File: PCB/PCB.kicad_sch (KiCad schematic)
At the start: 20 parts, among them SW1 SW_Push, SW2 SW_Push, SW3 SW_Push, SW4 SW_Push, SW5 SW_Push, SW6 SW_Push, U1 NodeMCU_1.0_(ESP-12E)

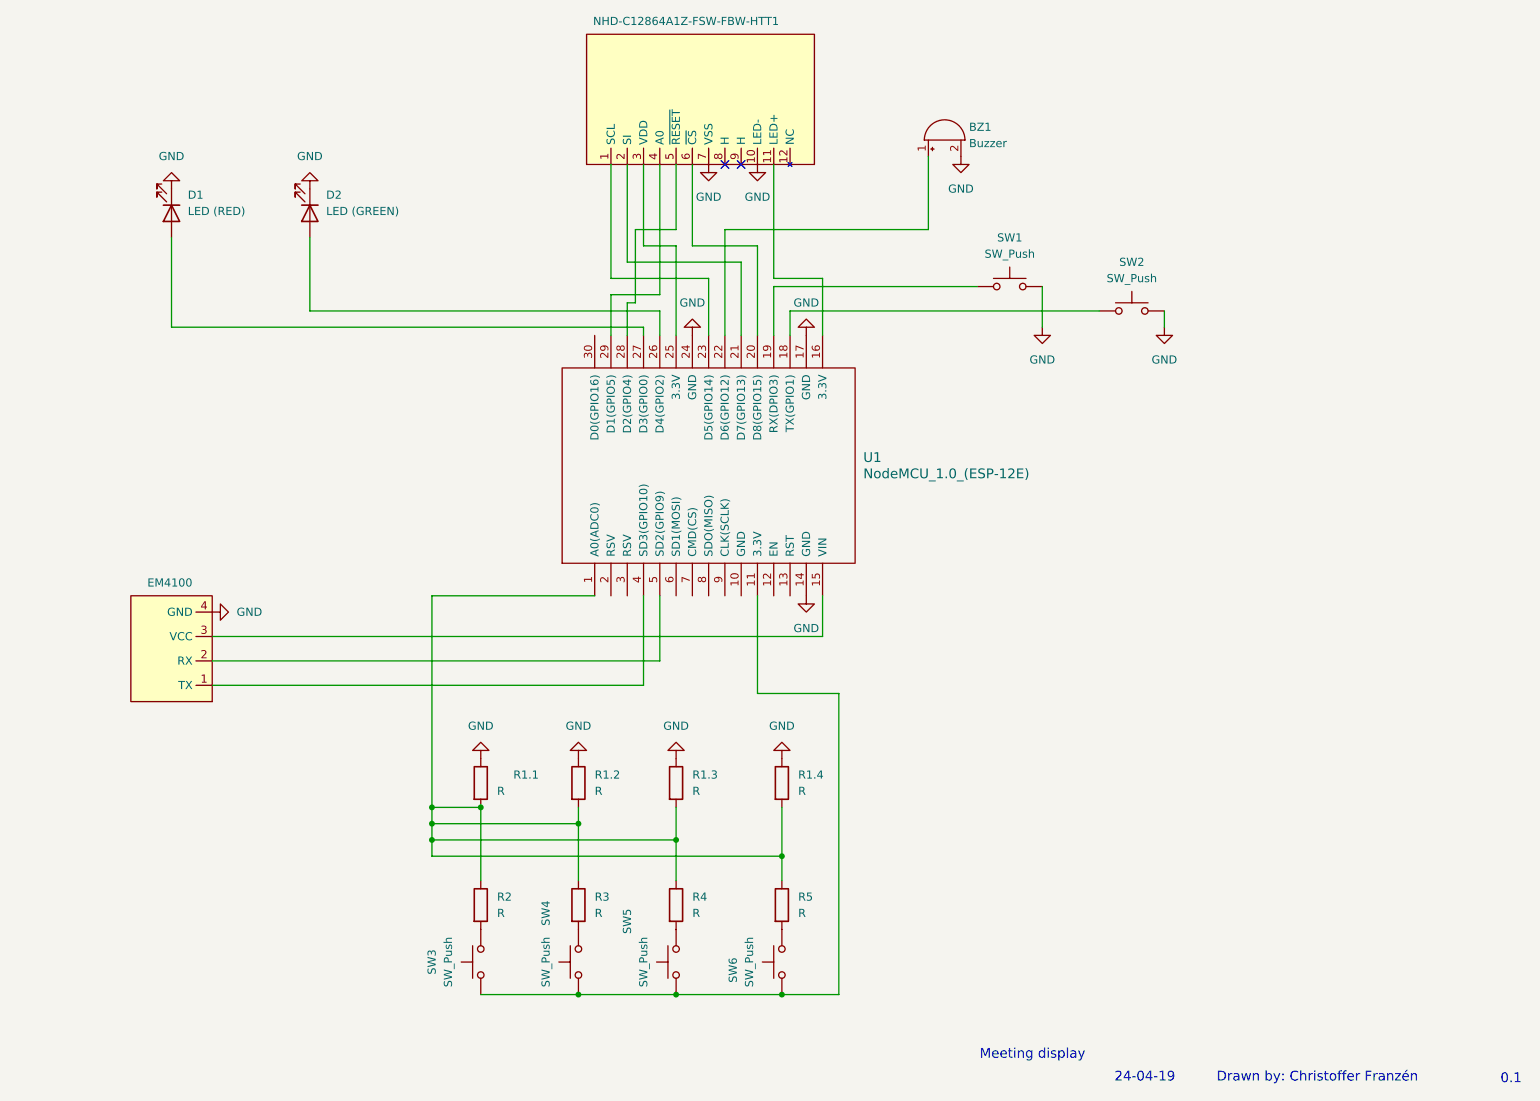
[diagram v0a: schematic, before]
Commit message: updated scematic and added footprints
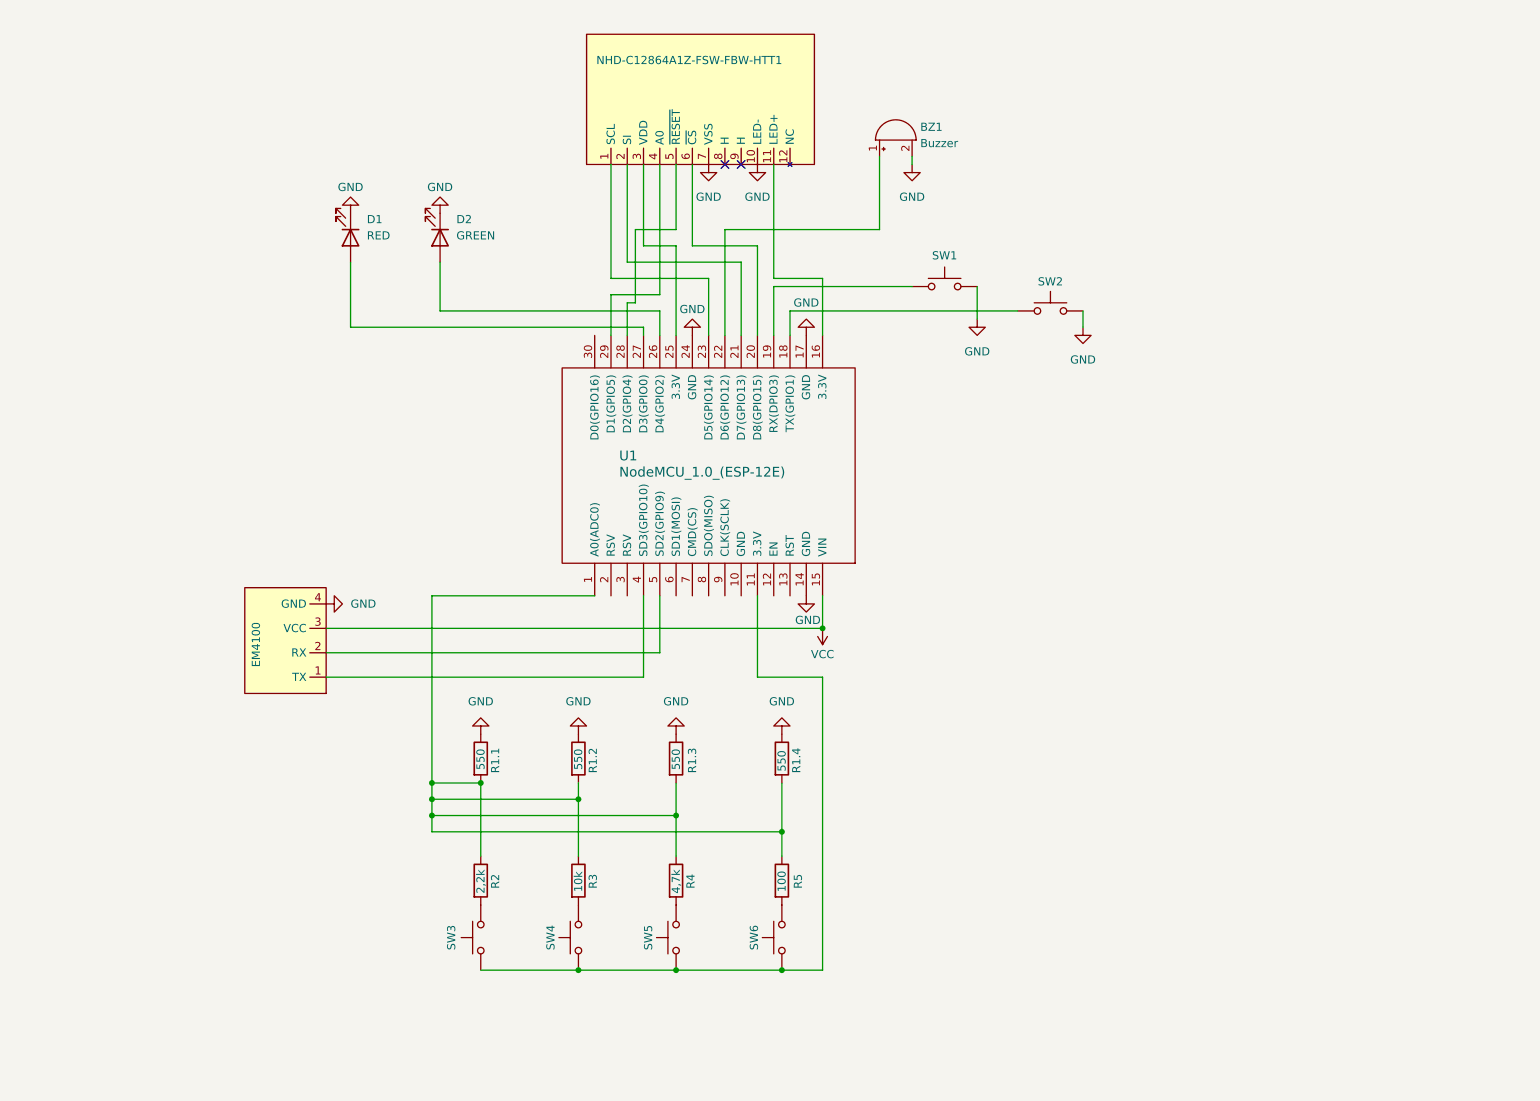
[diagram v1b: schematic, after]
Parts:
- BZ1: footprint (none) -> Buzzer_Beeper:Buzzer_12x9.5RM7.6
- D1: value LED (RED) -> RED; footprint (none) -> Diode_SMD:D_1206_3216Metric_Pad1.42x1.75mm_HandSolder
- D2: value LED (GREEN) -> GREEN; footprint (none) -> Diode_SMD:D_1206_3216Metric_Pad1.42x1.75mm_HandSolder
- EM4100: footprint (none) -> Connector:NS-Tech_Grove_1x04_P2mm_Vertical
- R1.1, R1.2, R1.3, R1.4: value R -> 550; footprint (none) -> Resistor_SMD:R_1206_3216Metric_Pad1.30x1.75mm_HandSolder
- R2: value R -> 2,2k; footprint (none) -> Resistor_SMD:R_1206_3216Metric_Pad1.30x1.75mm_HandSolder
- R3: value R -> 10k; footprint (none) -> Resistor_SMD:R_1206_3216Metric_Pad1.30x1.75mm_HandSolder
- R4: value R -> 4,7k; footprint (none) -> Resistor_SMD:R_1206_3216Metric_Pad1.30x1.75mm_HandSolder
- R5: value R -> 100; footprint (none) -> Resistor_SMD:R_1206_3216Metric_Pad1.30x1.75mm_HandSolder
- SW1, SW2, SW3, SW4, SW5, SW6: footprint (none) -> Button_Switch_SMD:SW_Push_SPST_NO_Alps_SKRK
- U1: footprint (none) -> 113990105:NodeMCU
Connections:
- net VCC: now reaches EM4100.3 (VCC), U1.15 (VIN)
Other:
- note removed: "0.1"
- note removed: "24-04-19"
- note removed: "Drawn by: Christoffer Franzén"
- note removed: "Meeting display"
- company: (none) -> KTH
- title: (none) -> Meeting display
- moved on the sheet: BZ1, D1, D2, EM4100, R1.1, R1.2, R1.3, R1.4, R2, R3, R4, R5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

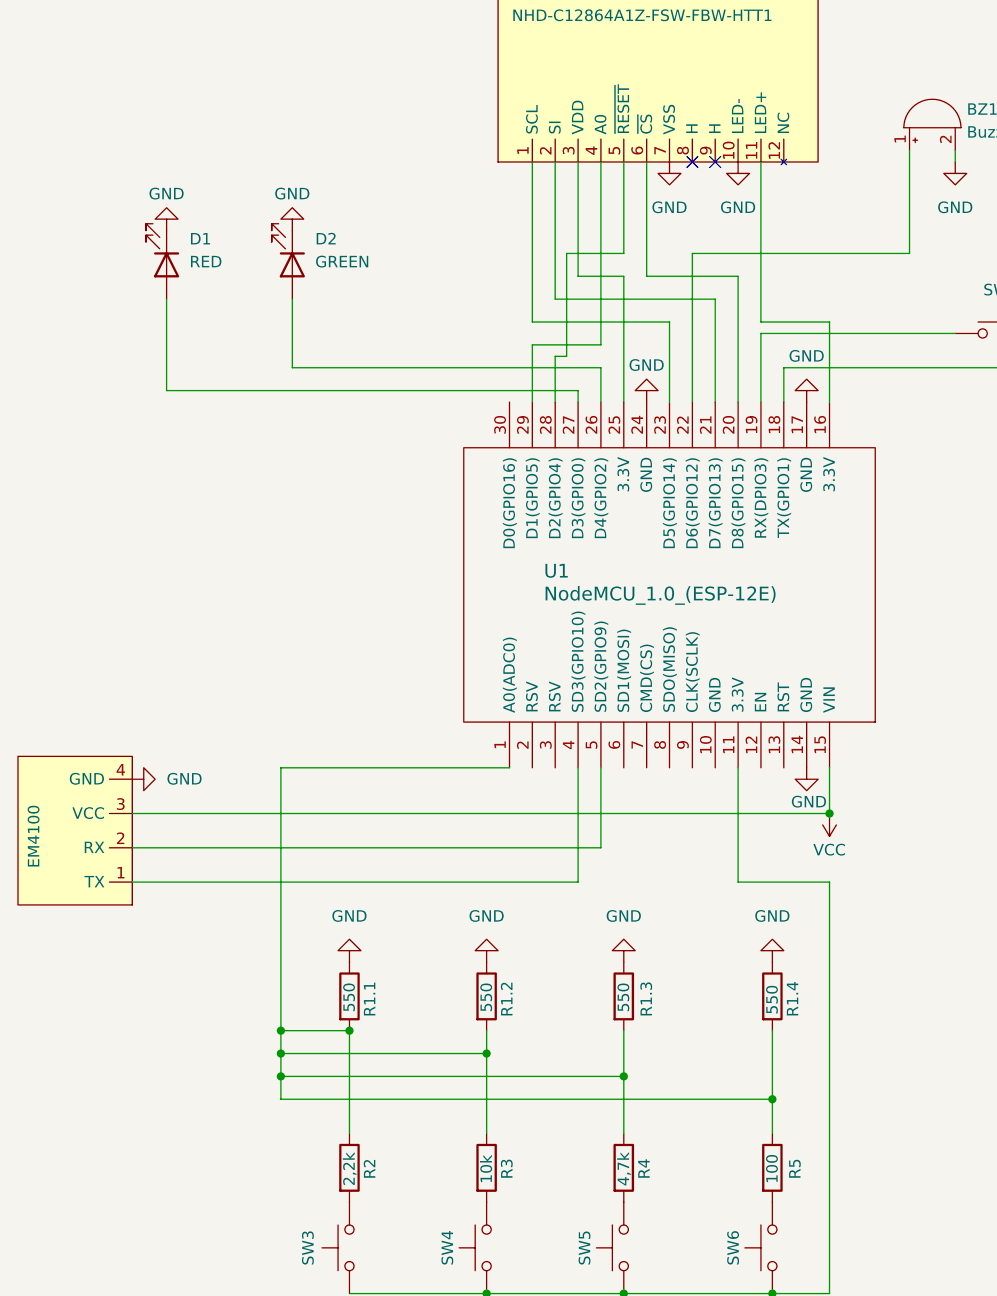
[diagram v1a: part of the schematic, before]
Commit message: version 0.2 removed resistor and 3v run
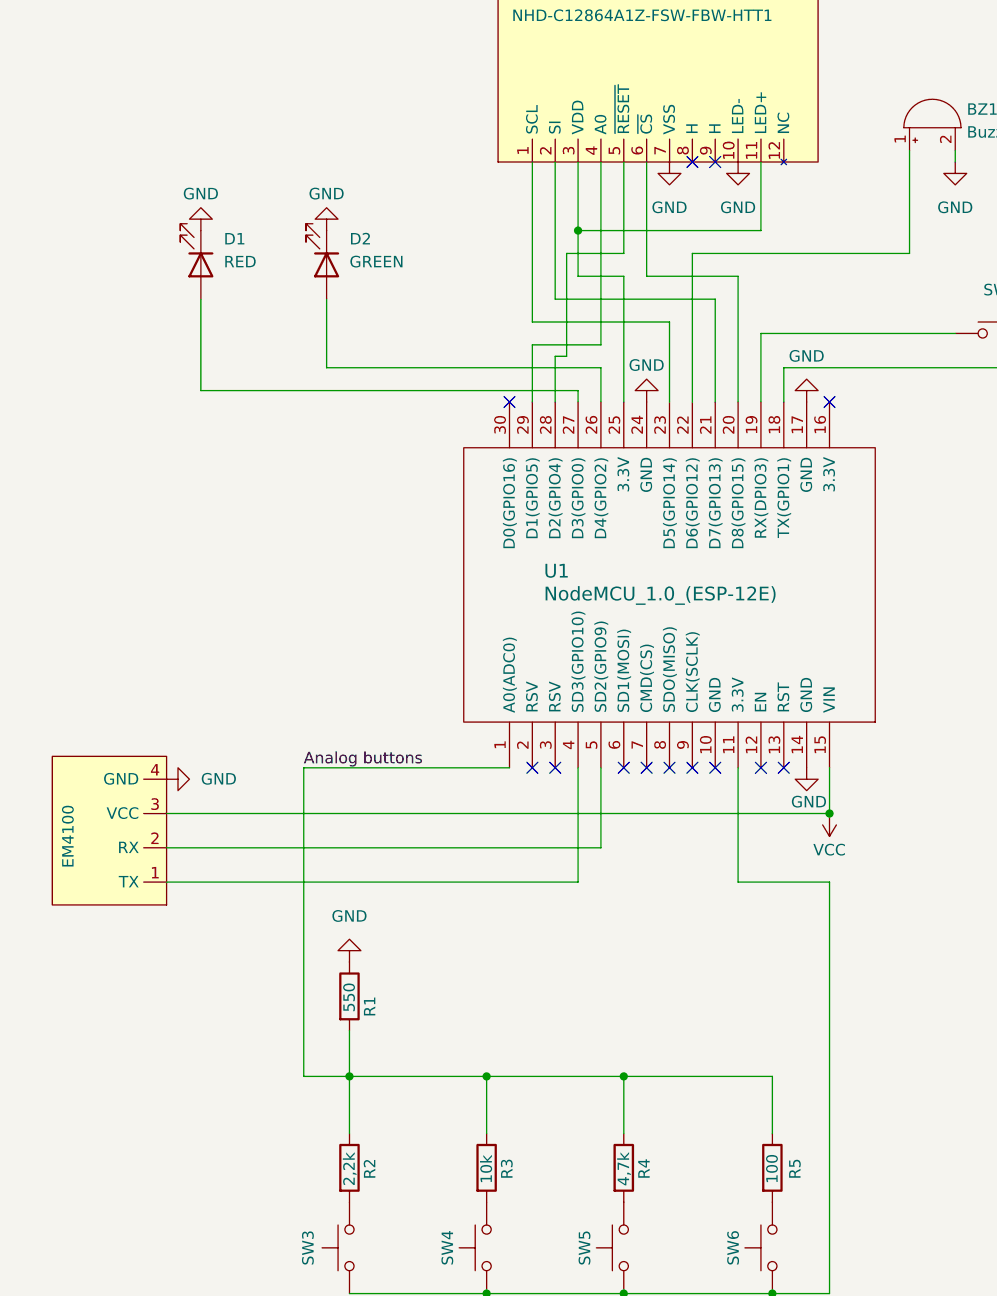
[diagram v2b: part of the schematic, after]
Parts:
- removed R1.2, R1.3, R1.4: 550, Resistor_SMD:R_1206_3216Metric_Pad1.30x1.75mm_HandSolder, symbol Device:R
- NHD-C12864A1Z-FSW-FBW-HTT1: footprint (none) -> Connector_PinHeader_1.27mm:PinHeader_1x30_P1.27mm_Horizontal
- renumbered R1.1 to R1
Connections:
- net Analog buttons: now reaches R1.2, R2.1, R3.1, R4.1, R5.1, U1.1 (A0(ADC0))
- net at NHD-C12864A1Z-FSW-FBW-HTT1.11 (LED+): now also NHD-C12864A1Z-FSW-FBW-HTT1.3 (VDD), U1.25 (3.3V); no longer U1.16 (3.3V)
- no-connect marks 2 -> 13
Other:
- moved on the sheet: D1, D2, EM4100

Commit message: added screen and button footprints
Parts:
- D1, D2: footprint Diode_SMD:D_1206_3216Metric_Pad1.42x1.75mm_HandSolder -> LED_THT:LED_D5.0mm
- NHD-C12864A1Z-FSW-FBW-HTT1: footprint Connector_PinHeader_1.27mm:PinHeader_1x30_P1.27mm_Horizontal -> Custom:NHD
- SW1, SW2, SW3, SW4, SW5, SW6: footprint Button_Switch_SMD:SW_Push_SPST_NO_Alps_SKRK -> Custom:SW_BUTT-2
- U1: footprint 113990105:NodeMCU -> Custom:NodeMCU
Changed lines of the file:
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@@
 			)
 		)
-		(property "Footprint" "Diode_SMD:D_1206_3216Metric_Pad1.42x1.75mm_HandSolder"
+		(property "Footprint" "LED_THT:LED_D5.0mm"
 			(at 92.71 62.23 0)
 			(effects
@@
 			)
 		)
-		(property "Footprint" "Button_Switch_SMD:SW_Push_SPST_NO_Alps_SKRK"
+		(property "Footprint" "Custom:SW_BUTT-2"
 			(at 181.61 64.77 0)
 			(effects
@@
 			)
 		)
-		(property "Footprint" "Connector_PinHeader_1.27mm:PinHeader_1x30_P1.27mm_Horizontal"
+		(property "Footprint" "Custom:NHD"
 			(at 128.778 14.986 0)
 			(effects
@@
 			)
 		)
-		(property "Footprint" "Button_Switch_SMD:SW_Push_SPST_NO_Alps_SKRK"
+		(property "Footprint" "Custom:SW_BUTT-2"
 			(at 151.13 171.45 0)
 			(effects
@@
 			)
 		)
-		(property "Footprint" "Button_Switch_SMD:SW_Push_SPST_NO_Alps_SKRK"
+		(property "Footprint" "Custom:SW_BUTT-2"
 			(at 198.12 68.58 0)
 			(effects
@@
 			)
 		)
-		(property "Footprint" "Button_Switch_SMD:SW_Push_SPST_NO_Alps_SKRK"
+		(property "Footprint" "Custom:SW_BUTT-2"
 			(at 134.62 171.45 0)
 			(effects
@@
 			)
 		)
-		(property "Footprint" "Button_Switch_SMD:SW_Push_SPST_NO_Alps_SKRK"
+		(property "Footprint" "Custom:SW_BUTT-2"
 			(at 119.38 171.45 0)
 			(effects
@@
 			)
 		)
-		(property "Footprint" "Button_Switch_SMD:SW_Push_SPST_NO_Alps_SKRK"
+		(property "Footprint" "Custom:SW_BUTT-2"
 			(at 104.14 171.45 0)
 			(effects
@@
 			)
 		)
-		(property "Footprint" "113990105:NodeMCU"
+		(property "Footprint" "Custom:NodeMCU"
 			(at 166.37 113.03 0)
 			(effects
@@
 			)
 		)
-		(property "Footprint" "Diode_SMD:D_1206_3216Metric_Pad1.42x1.75mm_HandSolder"
+		(property "Footprint" "LED_THT:LED_D5.0mm"
 			(at 106.68 62.23 0)
 			(effects

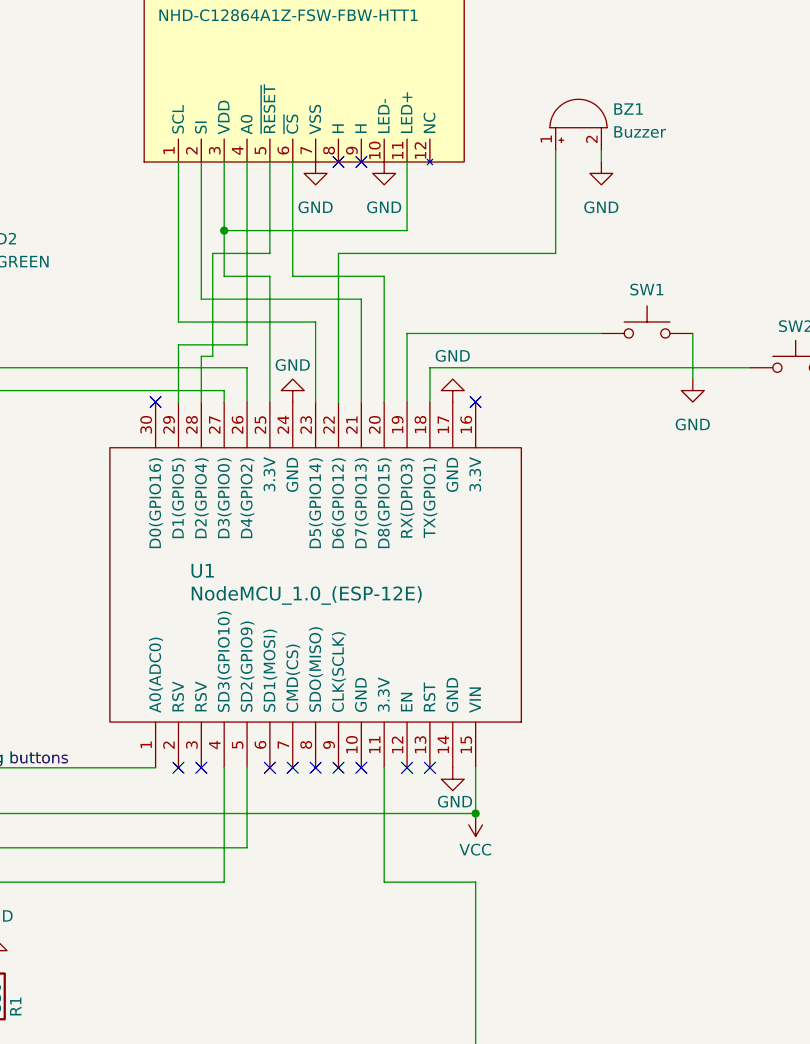
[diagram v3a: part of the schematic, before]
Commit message: done pcb drawing
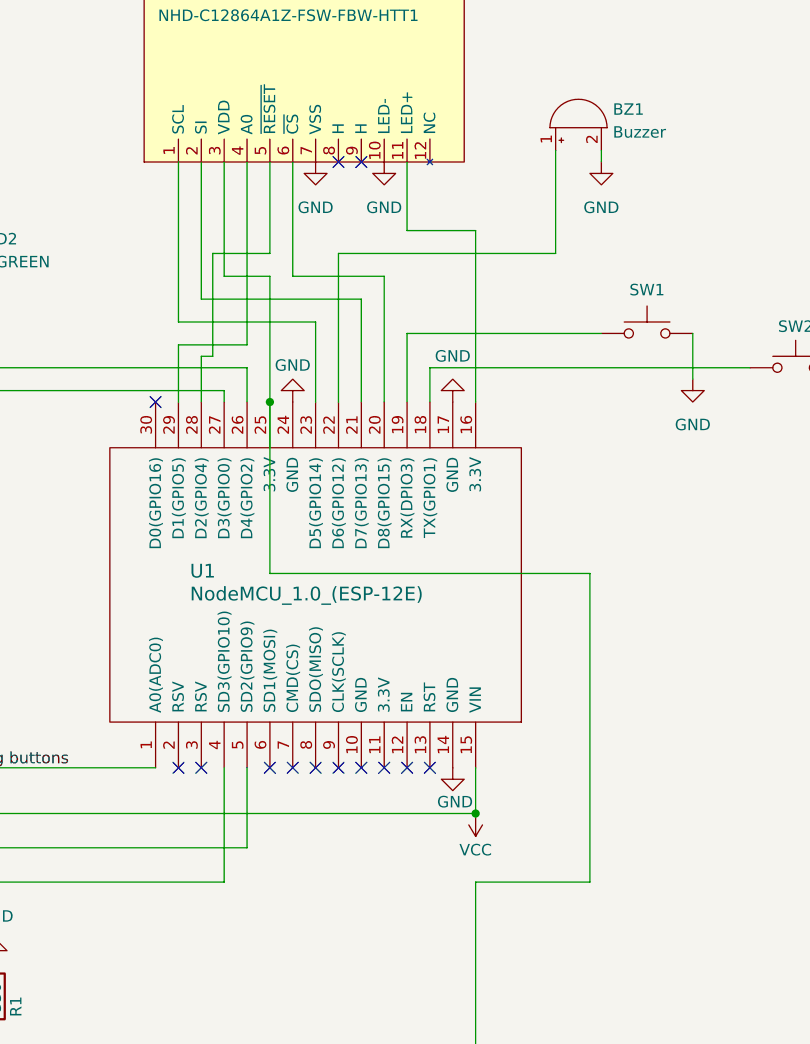
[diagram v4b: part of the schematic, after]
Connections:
- net at NHD-C12864A1Z-FSW-FBW-HTT1.3 (VDD), U1.25 (3.3V): now also SW3.1, SW4.1, SW5.1, SW6.1; no longer NHD-C12864A1Z-FSW-FBW-HTT1.11 (LED+)
- net at U1.16 (3.3V): now also NHD-C12864A1Z-FSW-FBW-HTT1.11 (LED+)
- now unconnected: U1.11 (3.3V)
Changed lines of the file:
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@@
-	)
-	(junction
-		(at 134.62 58.42)
-		(diameter 0)
-		(color 0 0 0 0)
 	)
 	(junction
@@
 	)
 	(junction
+		(at 139.7 77.47)
+		(diameter 0)
+		(color 0 0 0 0)
+	)
+	(junction
 		(at 109.22 152.4)
 		(diameter 0)
@@
 	)
 	(no_connect
+		(at 152.4 118.11)
+	)
+	(no_connect
 		(at 147.32 118.11)
 	)
@@
 	)
 	(no_connect
-		(at 162.56 77.47)
-	)
-	(no_connect
 		(at 149.86 50.8)
 	)
@@
 	(wire
 		(pts
+			(xy 162.56 58.42) (xy 154.94 58.42)
+		)
+		(stroke
+			(width 0)
+			(type default)
+		)
+	)
+	(wire
+		(pts
 			(xy 106.68 73.66) (xy 137.16 73.66)
 		)
@@
 	(wire
 		(pts
+			(xy 162.56 77.47) (xy 162.56 58.42)
+		)
+		(stroke
+			(width 0)
+			(type default)
+		)
+	)
+	(wire
+		(pts
 			(xy 156.21 176.53) (xy 162.56 176.53)
 		)
@@
 	(wire
 		(pts
+			(xy 162.56 130.81) (xy 175.26 130.81)
+		)
+		(stroke
+			(width 0)
+			(type default)
+		)
+	)
+	(wire
+		(pts
 			(xy 134.62 76.2) (xy 92.71 76.2)
 		)
@@
 	(wire
 		(pts
-			(xy 162.56 130.81) (xy 152.4 130.81)
-		)
-		(stroke
-			(width 0)
-			(type default)
-		)
-	)
-	(wire
-		(pts
 			(xy 154.94 77.47) (xy 154.94 69.85)
 		)
@@
 	(wire
 		(pts
-			(xy 134.62 58.42) (xy 134.62 50.8)
+			(xy 134.62 50.8) (xy 134.62 63.5)
 		)
 		(stroke
@@
 	(wire
 		(pts
+			(xy 139.7 96.52) (xy 139.7 77.47)
+		)
+		(stroke
+			(width 0)
+			(type default)
+		)
+	)
+	(wire
+		(pts
 			(xy 129.54 68.58) (xy 144.78 68.58)
 		)
@@
 	(wire
 		(pts
+			(xy 175.26 96.52) (xy 139.7 96.52)
+		)
+		(stroke
+			(width 0)
+			(type default)
+		)
+	)
+	(wire
+		(pts
 			(xy 134.62 77.47) (xy 134.62 76.2)
 		)
@@
 	(wire
 		(pts
-			(xy 134.62 63.5) (xy 134.62 58.42)
-		)
-		(stroke
-			(width 0)
-			(type default)
-		)
-	)
-	(wire
-		(pts
 			(xy 137.16 71.12) (xy 129.54 71.12)
 		)
@@
 	(wire
 		(pts
-			(xy 152.4 118.11) (xy 152.4 130.81)
-		)
-		(stroke
-			(width 0)
-			(type default)
-		)
-	)
-	(wire
-		(pts
 			(xy 139.7 152.4) (xy 156.21 152.4)
 		)
@@
 	(wire
 		(pts
+			(xy 175.26 130.81) (xy 175.26 96.52)
+		)
+		(stroke
+			(width 0)
+			(type default)
+		)
+	)
+	(wire
+		(pts
 			(xy 139.7 77.47) (xy 139.7 63.5)
 		)
@@
 		)
 		(stroke
-			(width 0)
-			(type default)
-		)
-	)
-	(wire
-		(pts
-			(xy 134.62 58.42) (xy 154.94 58.42)
-		)
-		(stroke
